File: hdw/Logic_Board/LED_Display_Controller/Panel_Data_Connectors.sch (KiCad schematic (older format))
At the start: 11 parts, among them J2901 STRING 1, J2902 STRING 2, J2903 STRING 3, J2904 STRING 4

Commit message: Added some digikey partnumbers to components
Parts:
- D2901, D2902, D2903, D2904, D2905, D2906, D2907: Digi-Key PN (none) -> F3160CT-ND
- J2901, J2902, J2903, J2904: Digi-Key PN (none) -> ED10523-ND
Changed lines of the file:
@@
 F 2 "" H 2550 1800 50  0001 C CNN
 F 3 "~" H 2550 1800 50  0001 C CNN
+F 4 "ED10523-ND" H 0   0   50  0001 C CNN "Digi-Key PN"
 	1    2550 1800
 	1    0    0    -1
@@
 F 2 "" H 2550 3300 50  0001 C CNN
 F 3 "~" H 2550 3300 50  0001 C CNN
+F 4 "ED10523-ND" H 0   0   50  0001 C CNN "Digi-Key PN"
 	1    2550 3300
 	1    0    0    -1
@@
 F 2 "" H 2550 4800 50  0001 C CNN
 F 3 "~" H 2550 4800 50  0001 C CNN
+F 4 "ED10523-ND" H 0   0   50  0001 C CNN "Digi-Key PN"
 	1    2550 4800
 	1    0    0    -1
@@
 F 2 "" H 2550 6300 50  0001 C CNN
 F 3 "~" H 2550 6300 50  0001 C CNN
+F 4 "ED10523-ND" H 0   0   50  0001 C CNN "Digi-Key PN"
 	1    2550 6300
 	1    0    0    -1
@@
 F 2 "Package_TO_SOT_SMD:SOT-363_SC-70-6" H 4990 2510 50  0001 L CNN
 F 3 "http://www.littelfuse.com/~/media/files/littelfuse/technical%20resources/documents/data%20sheets/sp05xxba.pdf" H 4815 2685 50  0001 C CNN
+F 4 "F3160CT-ND" H 0   0   50  0001 C CNN "Digi-Key PN"
 	1    4690 2560
 	1    0    0    -1
@@
 F 2 "Package_TO_SOT_SMD:SOT-363_SC-70-6" H 6180 2510 50  0001 L CNN
 F 3 "http://www.littelfuse.com/~/media/files/littelfuse/technical%20resources/documents/data%20sheets/sp05xxba.pdf" H 6005 2685 50  0001 C CNN
+F 4 "F3160CT-ND" H 0   0   50  0001 C CNN "Digi-Key PN"
 	1    5880 2560
 	1    0    0    -1
@@
 F 2 "Package_TO_SOT_SMD:SOT-363_SC-70-6" H 7370 2510 50  0001 L CNN
 F 3 "http://www.littelfuse.com/~/media/files/littelfuse/technical%20resources/documents/data%20sheets/sp05xxba.pdf" H 7195 2685 50  0001 C CNN
+F 4 "F3160CT-ND" H 0   0   50  0001 C CNN "Digi-Key PN"
 	1    7070 2560
 	1    0    0    -1
@@
 F 2 "Package_TO_SOT_SMD:SOT-363_SC-70-6" H 8560 2510 50  0001 L CNN
 F 3 "http://www.littelfuse.com/~/media/files/littelfuse/technical%20resources/documents/data%20sheets/sp05xxba.pdf" H 8385 2685 50  0001 C CNN
+F 4 "F3160CT-ND" H 0   0   50  0001 C CNN "Digi-Key PN"
 	1    8260 2560
 	1    0    0    -1
@@
 F 2 "Package_TO_SOT_SMD:SOT-363_SC-70-6" H 4990 3800 50  0001 L CNN
 F 3 "http://www.littelfuse.com/~/media/files/littelfuse/technical%20resources/documents/data%20sheets/sp05xxba.pdf" H 4815 3975 50  0001 C CNN
+F 4 "F3160CT-ND" H 0   0   50  0001 C CNN "Digi-Key PN"
 	1    4690 3850
 	1    0    0    -1
@@
 F 2 "Package_TO_SOT_SMD:SOT-363_SC-70-6" H 6180 3800 50  0001 L CNN
 F 3 "http://www.littelfuse.com/~/media/files/littelfuse/technical%20resources/documents/data%20sheets/sp05xxba.pdf" H 6005 3975 50  0001 C CNN
+F 4 "F3160CT-ND" H 0   0   50  0001 C CNN "Digi-Key PN"
 	1    5880 3850
 	1    0    0    -1
@@
 F 2 "Package_TO_SOT_SMD:SOT-363_SC-70-6" H 9830 2510 50  0001 L CNN
 F 3 "http://www.littelfuse.com/~/media/files/littelfuse/technical%20resources/documents/data%20sheets/sp05xxba.pdf" H 9655 2685 50  0001 C CNN
+F 4 "F3160CT-ND" H 0   0   50  0001 C CNN "Digi-Key PN"
 	1    9530 2560
 	1    0    0    -1

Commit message: First pass assignment of footprints to all components
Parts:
- D2901, D2902, D2903, D2904, D2905, D2906, D2907: footprint Package_TO_SOT_SMD:SOT-363_SC-70-6 -> TO_SOT_Packages_SMD:SOT-363_SC-70-6
- J2901, J2902, J2903, J2904: footprint (none) -> Connectors_IDC:IDC-Header_2x08_Pitch2.54mm_Straight
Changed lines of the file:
@@
 F 0 "J2901" H 2600 2317 50  0000 C CNN
 F 1 "STRING 1" H 2600 2226 50  0000 C CNN
-F 2 "" H 2550 1800 50  0001 C CNN
+F 2 "Connectors_IDC:IDC-Header_2x08_Pitch2.54mm_Straight" H 2550 1800 50  0001 C CNN
 F 3 "~" H 2550 1800 50  0001 C CNN
 F 4 "ED10523-ND" H 0   0   50  0001 C CNN "Digi-Key PN"
@@
 F 0 "J2902" H 2600 3817 50  0000 C CNN
 F 1 "STRING 2" H 2600 3726 50  0000 C CNN
-F 2 "" H 2550 3300 50  0001 C CNN
+F 2 "Connectors_IDC:IDC-Header_2x08_Pitch2.54mm_Straight" H 2550 3300 50  0001 C CNN
 F 3 "~" H 2550 3300 50  0001 C CNN
 F 4 "ED10523-ND" H 0   0   50  0001 C CNN "Digi-Key PN"
@@
 F 0 "J2903" H 2600 5317 50  0000 C CNN
 F 1 "STRING 3" H 2600 5226 50  0000 C CNN
-F 2 "" H 2550 4800 50  0001 C CNN
+F 2 "Connectors_IDC:IDC-Header_2x08_Pitch2.54mm_Straight" H 2550 4800 50  0001 C CNN
 F 3 "~" H 2550 4800 50  0001 C CNN
 F 4 "ED10523-ND" H 0   0   50  0001 C CNN "Digi-Key PN"
@@
 F 0 "J2904" H 2600 6817 50  0000 C CNN
 F 1 "STRING 4" H 2600 6726 50  0000 C CNN
-F 2 "" H 2550 6300 50  0001 C CNN
+F 2 "Connectors_IDC:IDC-Header_2x08_Pitch2.54mm_Straight" H 2550 6300 50  0001 C CNN
 F 3 "~" H 2550 6300 50  0001 C CNN
 F 4 "ED10523-ND" H 0   0   50  0001 C CNN "Digi-Key PN"
@@
 F 0 "D2901" H 4990 2660 50  0000 L CNN
 F 1 "SP0505BAJT" H 4990 2585 50  0000 L CNN
-F 2 "Package_TO_SOT_SMD:SOT-363_SC-70-6" H 4990 2510 50  0001 L CNN
+F 2 "TO_SOT_Packages_SMD:SOT-363_SC-70-6" H 4990 2510 50  0001 L CNN
 F 3 "http://www.littelfuse.com/~/media/files/littelfuse/technical%20resources/documents/data%20sheets/sp05xxba.pdf" H 4815 2685 50  0001 C CNN
 F 4 "F3160CT-ND" H 0   0   50  0001 C CNN "Digi-Key PN"
@@
 F 0 "D2903" H 6180 2660 50  0000 L CNN
 F 1 "SP0505BAJT" H 6180 2585 50  0000 L CNN
-F 2 "Package_TO_SOT_SMD:SOT-363_SC-70-6" H 6180 2510 50  0001 L CNN
+F 2 "TO_SOT_Packages_SMD:SOT-363_SC-70-6" H 6180 2510 50  0001 L CNN
 F 3 "http://www.littelfuse.com/~/media/files/littelfuse/technical%20resources/documents/data%20sheets/sp05xxba.pdf" H 6005 2685 50  0001 C CNN
 F 4 "F3160CT-ND" H 0   0   50  0001 C CNN "Digi-Key PN"
@@
 F 0 "D2905" H 7370 2660 50  0000 L CNN
 F 1 "SP0505BAJT" H 7370 2585 50  0000 L CNN
-F 2 "Package_TO_SOT_SMD:SOT-363_SC-70-6" H 7370 2510 50  0001 L CNN
+F 2 "TO_SOT_Packages_SMD:SOT-363_SC-70-6" H 7370 2510 50  0001 L CNN
 F 3 "http://www.littelfuse.com/~/media/files/littelfuse/technical%20resources/documents/data%20sheets/sp05xxba.pdf" H 7195 2685 50  0001 C CNN
 F 4 "F3160CT-ND" H 0   0   50  0001 C CNN "Digi-Key PN"
@@
 F 0 "D2906" H 8560 2660 50  0000 L CNN
 F 1 "SP0505BAJT" H 8560 2585 50  0000 L CNN
-F 2 "Package_TO_SOT_SMD:SOT-363_SC-70-6" H 8560 2510 50  0001 L CNN
+F 2 "TO_SOT_Packages_SMD:SOT-363_SC-70-6" H 8560 2510 50  0001 L CNN
 F 3 "http://www.littelfuse.com/~/media/files/littelfuse/technical%20resources/documents/data%20sheets/sp05xxba.pdf" H 8385 2685 50  0001 C CNN
 F 4 "F3160CT-ND" H 0   0   50  0001 C CNN "Digi-Key PN"
@@
 F 0 "D2902" H 4990 3950 50  0000 L CNN
 F 1 "SP0505BAJT" H 4990 3875 50  0000 L CNN
-F 2 "Package_TO_SOT_SMD:SOT-363_SC-70-6" H 4990 3800 50  0001 L CNN
+F 2 "TO_SOT_Packages_SMD:SOT-363_SC-70-6" H 4990 3800 50  0001 L CNN
 F 3 "http://www.littelfuse.com/~/media/files/littelfuse/technical%20resources/documents/data%20sheets/sp05xxba.pdf" H 4815 3975 50  0001 C CNN
 F 4 "F3160CT-ND" H 0   0   50  0001 C CNN "Digi-Key PN"
@@
 F 0 "D2904" H 6180 3950 50  0000 L CNN
 F 1 "SP0505BAJT" H 6180 3875 50  0000 L CNN
-F 2 "Package_TO_SOT_SMD:SOT-363_SC-70-6" H 6180 3800 50  0001 L CNN
+F 2 "TO_SOT_Packages_SMD:SOT-363_SC-70-6" H 6180 3800 50  0001 L CNN
 F 3 "http://www.littelfuse.com/~/media/files/littelfuse/technical%20resources/documents/data%20sheets/sp05xxba.pdf" H 6005 3975 50  0001 C CNN
 F 4 "F3160CT-ND" H 0   0   50  0001 C CNN "Digi-Key PN"
@@
 F 0 "D2907" H 9830 2660 50  0000 L CNN
 F 1 "SP0505BAJT" H 9830 2585 50  0000 L CNN
-F 2 "Package_TO_SOT_SMD:SOT-363_SC-70-6" H 9830 2510 50  0001 L CNN
+F 2 "TO_SOT_Packages_SMD:SOT-363_SC-70-6" H 9830 2510 50  0001 L CNN
 F 3 "http://www.littelfuse.com/~/media/files/littelfuse/technical%20resources/documents/data%20sheets/sp05xxba.pdf" H 9655 2685 50  0001 C CNN
 F 4 "F3160CT-ND" H 0   0   50  0001 C CNN "Digi-Key PN"

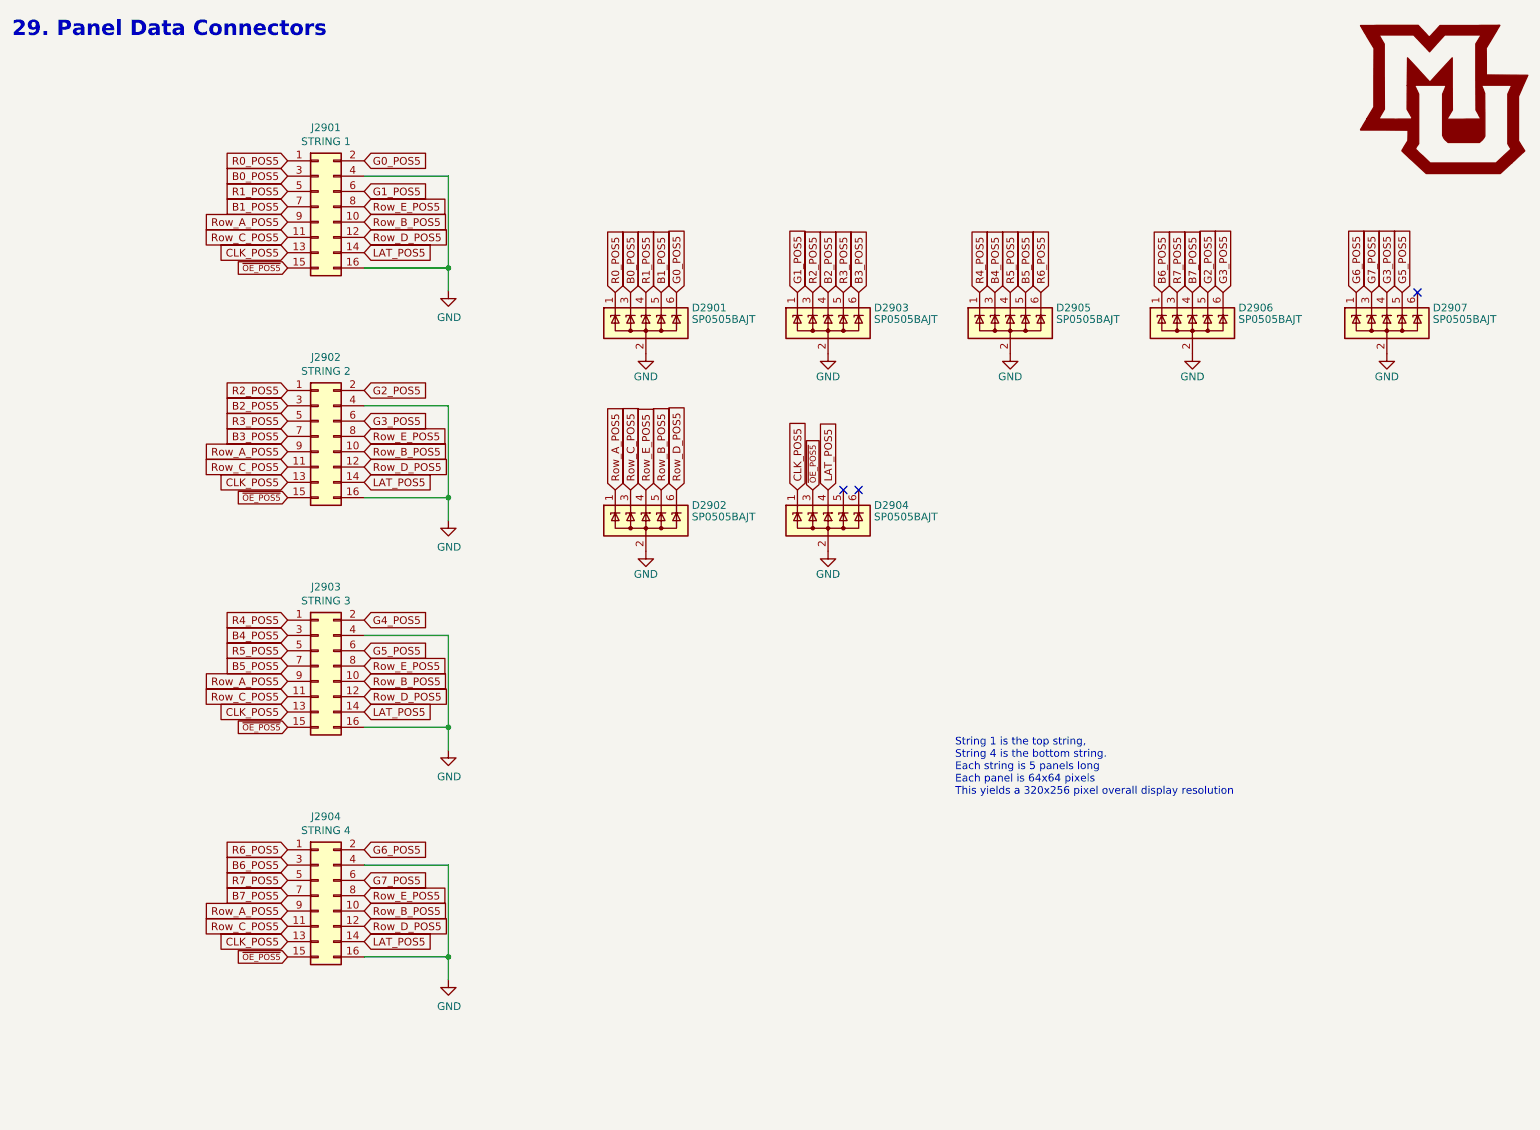
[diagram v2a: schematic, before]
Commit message: Corrected output data TVS diodes
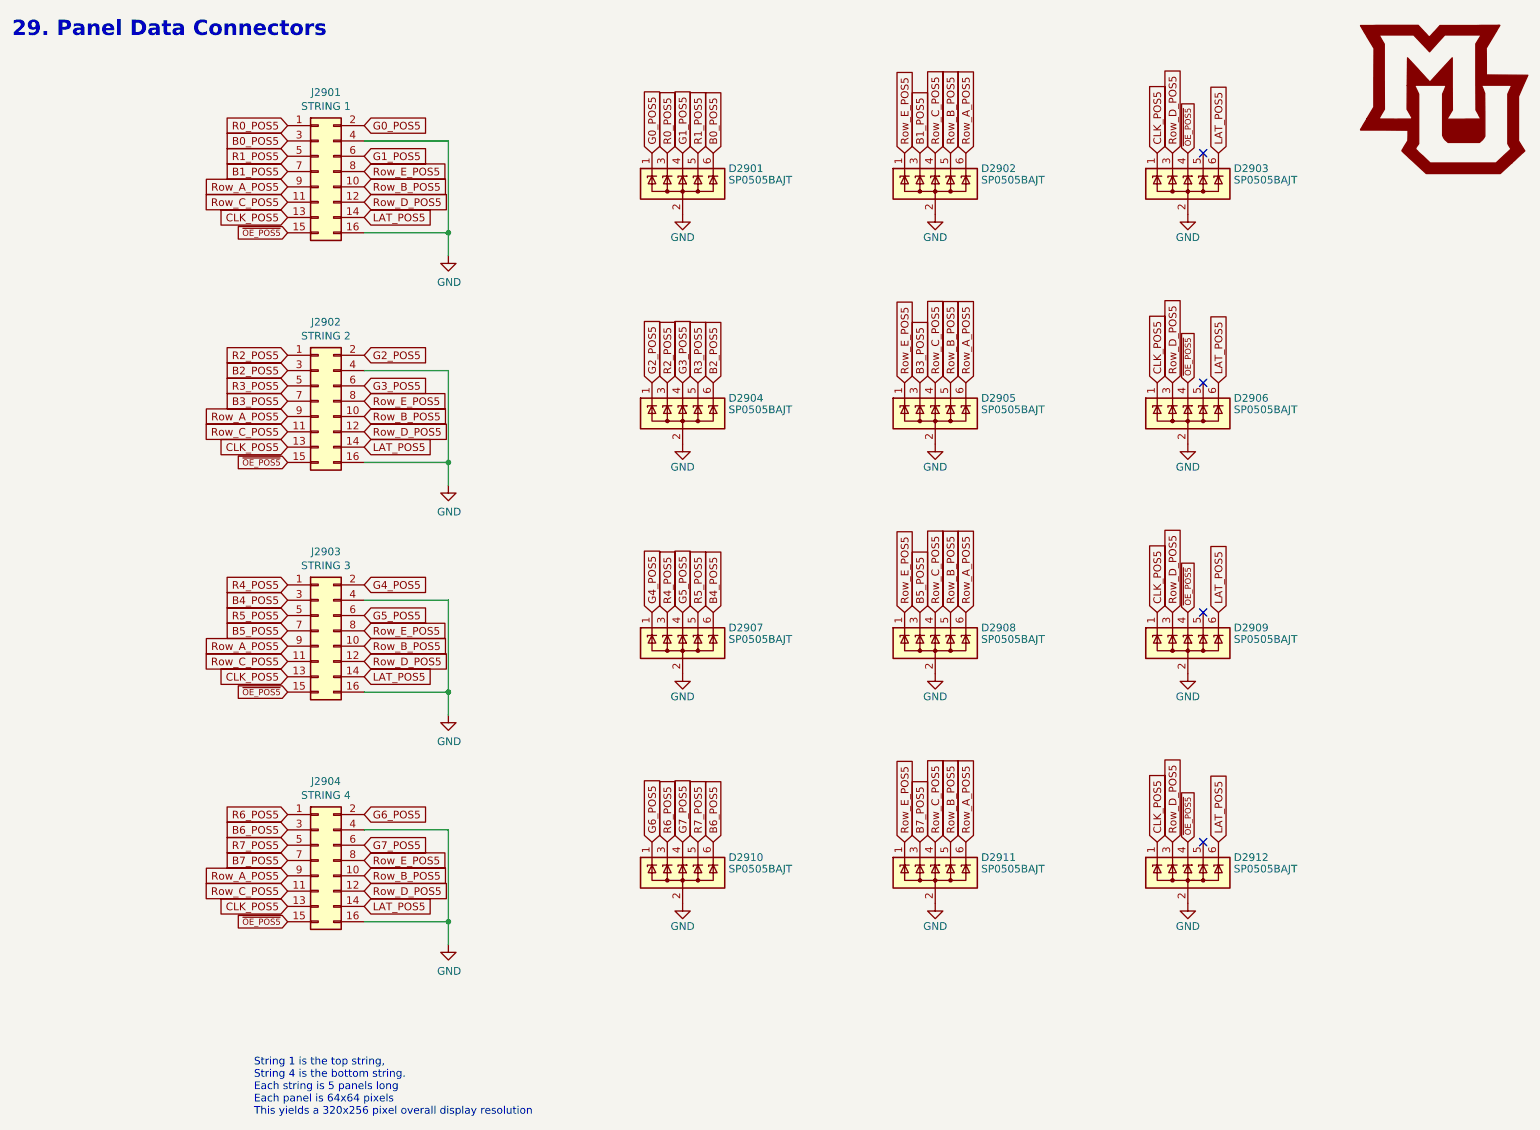
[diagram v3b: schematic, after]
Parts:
- added D2908, D2909, D2910, D2911, D2912: SP0505BAJT, TO_SOT_Packages_SMD:SOT-363_SC-70-6, symbol Power_Protection:SP0505BAJT
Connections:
- net B0_POS5: now also D2901.6 (K); no longer D2901.3 (K)
- net B1_POS5: now also D2902.3 (K); no longer D2901.5 (K)
- net B2_POS5: now also D2904.6 (K); no longer D2903.4 (K)
- net B3_POS5: now also D2905.3 (K); no longer D2903.6 (K)
- net B4_POS5: now also D2907.6 (K); no longer D2905.3 (K)
- net B5_POS5: now also D2908.3 (K); no longer D2905.5 (K)
- net B6_POS5: now also D2910.6 (K); no longer D2906.1 (K)
- net B7_POS5: now also D2911.3 (K); no longer D2906.4 (K)
- net CLK_POS5: now also D2903.1 (K), D2906.1 (K), D2909.1 (K), D2912.1 (K); no longer D2904.1 (K)
- net G0_POS5: now also D2901.1 (K); no longer D2901.6 (K)
- net G1_POS5: now also D2901.4 (K); no longer D2903.1 (K)
- net G2_POS5: now also D2904.1 (K); no longer D2906.5 (K)
- net G3_POS5: now also D2904.4 (K); no longer D2906.6 (K), D2907.4 (K)
- net G4_POS5: now also D2907.1 (K)
- net G5_POS5: now also D2907.4 (K); no longer D2907.5 (K)
- net G6_POS5: now also D2910.1 (K); no longer D2907.1 (K)
- net G7_POS5: now also D2910.4 (K); no longer D2907.3 (K)
- net GND: now also D2908.2 (A), D2909.2 (A), D2910.2 (A), D2911.2 (A), D2912.2 (A)
- net LAT_POS5: now also D2903.6 (K), D2906.6 (K), D2909.6 (K), D2912.6 (K); no longer D2904.4 (K)
- net R0_POS5: now also D2901.3 (K); no longer D2901.1 (K)
- net R1_POS5: now also D2901.5 (K); no longer D2901.4 (K)
- net R2_POS5: now also D2904.3 (K); no longer D2903.3 (K)
- net R3_POS5: now also D2904.5 (K); no longer D2903.5 (K)
- net R4_POS5: now also D2907.3 (K); no longer D2905.1 (K)
- net R5_POS5: now also D2907.5 (K); no longer D2905.4 (K)
- net R6_POS5: now also D2910.3 (K); no longer D2905.6 (K)
- net R7_POS5: now also D2910.5 (K); no longer D2906.3 (K)
- net Row_A_POS5: now also D2902.6 (K), D2905.6 (K), D2908.6 (K), D2911.6 (K); no longer D2902.1 (K)
- net Row_B_POS5: now also D2905.5 (K), D2908.5 (K), D2911.5 (K)
- net Row_C_POS5: now also D2902.4 (K), D2905.4 (K), D2908.4 (K), D2911.4 (K); no longer D2902.3 (K)
- net Row_D_POS5: now also D2903.3 (K), D2906.3 (K), D2909.3 (K), D2912.3 (K); no longer D2902.6 (K)
- net Row_E_POS5: now also D2902.1 (K), D2905.1 (K), D2908.1 (K), D2911.1 (K); no longer D2902.4 (K)
- net ~OE_POS5: now also D2903.4 (K), D2906.4 (K), D2909.4 (K), D2912.4 (K); no longer D2904.3 (K)
- no-connect marks 3 -> 4
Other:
- moved on the sheet: J2901, J2902, J2903, J2904
